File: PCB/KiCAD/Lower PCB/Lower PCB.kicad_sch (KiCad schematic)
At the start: 16 parts, among them J2 Conn_01x02, U1 ATmega328PB-A, Y1 Crystal

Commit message: Placed components on Lower PCB
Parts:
- R4: value 330 -> 10k
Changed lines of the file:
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@@
 			)
 		)
-		(property "Value" "330"
+		(property "Value" "10k"
 			(at 68.58 88.8999 0)
 			(effects

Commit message: More work to the lower PCB
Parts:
- removed Y1: Crystal, Crystal:Crystal_SMD_3225-4Pin_3.2x2.5mm_HandSoldering, symbol Device:Crystal
- added C31, C32: 100nF, Capacitor_SMD:C_0805_2012Metric_Pad1.18x1.45mm_HandSolder, symbol Device:C
- added D10, D11, D12, D13, D14, D15, D16, D17, D18, D19, D20, D21, D22, D23, D24, D5, D6, D7, D8, D9: LED, LED_SMD:LED_PLCC-2_3.4x3.0mm_KA, symbol Device:LED
- added IC1, IC2: ADG608BRZ, ADG608BRZ:SOIC127P600X175-16N, symbol ADG608BRZ:ADG608BRZ
- added Q1, Q10, Q11, Q12, Q13, Q14, Q15, Q16, Q2, Q3, Q4, Q5, Q6, Q7, Q8, Q9: SFH320, LED_SMD:LED_PLCC-2_3.4x3.0mm_KA, symbol Sensor_Optical:SFH320
- added R10, R14, R16, R18, R35, R36, R37, R38, R39, R40, R41, R42, R43, R44, R45, R46: 10k, Resistor_SMD:R_0805_2012Metric_Pad1.20x1.40mm_HandSolder, symbol Device:R
- added R11, R15, R17, R19, R20, R21, R22, R23, R24, R25, R26, R27, R28, R29, R30, R31, R32, R33, R34, R9: 330, Resistor_SMD:R_0805_2012Metric_Pad1.20x1.40mm_HandSolder, symbol Device:R
- added Y1: Crystal_GND24, Crystal:Crystal_SMD_5032-4Pin_5.0x3.2mm, symbol Device:Crystal_GND24
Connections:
- net +5V: now also C31.1, C32.1, IC1.13 (VDD), IC1.2 (EN), IC2.13 (VDD), IC2.2 (EN), Q1.1 (C), Q10.1 (C), Q11.1 (C), Q12.1 (C), Q13.1 (C), Q14.1 (C), Q15.1 (C), Q16.1 (C), Q2.1 (C), Q3.1 (C), Q4.1 (C), Q5.1 (C), Q6.1 (C), Q7.1 (C), Q8.1 (C), Q9.1 (C), R11.2, R15.2, R17.2, R19.2, R20.2, R21.2, R22.2, R23.2, R24.2, R25.2, R26.2, R27.2, R28.2, R29.2, R30.2, R31.2, R32.2, R33.2, R34.2, R9.2
- net GND: now also C31.2, C32.2, D10.1 (K), D11.1 (K), D12.1 (K), D13.1 (K), D14.1 (K), D15.1 (K), D16.1 (K), D17.1 (K), D18.1 (K), D19.1 (K), D20.1 (K), D21.1 (K), D22.1 (K), D23.1 (K), D24.1 (K), D5.1 (K), D6.1 (K), D7.1 (K), D8.1 (K), D9.1 (K), IC1.14 (GND), IC1.3 (VSS), IC2.14 (GND), IC2.3 (VSS), R10.1, R14.1, R16.1, R18.1, R35.1, R36.1, R37.1, R38.1, R39.1, R40.1, R41.1, R42.1, R43.1, R44.1, R45.1, R46.1
- net at C5.2, U1.8 (XTAL2/PB7): now also Y1.3
- net at C4.2, U1.7 (XTAL1/PB6): now also Y1.1
- new net: D7.2 (A), R15.1
- new net: IC1.4 (S1), Q1.2 (E), R10.2
- new net: D22.2 (A), R32.1
- new net: D23.2 (A), R33.1
- new net: D11.2 (A), R21.1
- new net: IC2.6 (S3), Q11.2 (E), R41.2
- new net: IC2.5 (S2), Q10.2 (E), R40.2
- new net: D19.2 (A), R29.1
- new net: D5.2 (A), R9.1
- new net: D14.2 (A), R24.1
- new net: IC1.5 (S2), Q2.2 (E), R14.2
- new net: D10.2 (A), R20.1
- new net: IC1.12 (S5), Q5.2 (E), R35.2
- new net: D13.2 (A), R23.1
- new net: IC2.7 (S4), Q12.2 (E), R42.2
- new net: IC2.11 (S6), Q14.2 (E), R44.2
- new net: IC1.9 (S8), Q8.2 (E), R38.2
- new net: D6.2 (A), R11.1
- new net: D9.2 (A), R19.1
- new net: D17.2 (A), R27.1
- new net: D21.2 (A), R31.1
- new net: D16.2 (A), R26.1
- new net: IC2.4 (S1), Q9.2 (E), R39.2
- new net: IC1.10 (S7), Q7.2 (E), R37.2
- new net: IC1.11 (S6), Q6.2 (E), R36.2
- new net: IC1.6 (S3), Q3.2 (E), R16.2
- new net: IC1.7 (S4), Q4.2 (E), R18.2
- new net: D8.2 (A), R17.1
- new net: D15.2 (A), R25.1
- new net: D12.2 (A), R22.1
- new net: D20.2 (A), R30.1
- new net: IC2.10 (S7), Q15.2 (E), R45.2
- new net: IC2.9 (S8), Q16.2 (E), R46.2
- new net: D24.2 (A), R34.1
- new net: D18.2 (A), R28.1
- new net: IC2.12 (S5), Q13.2 (E), R43.2

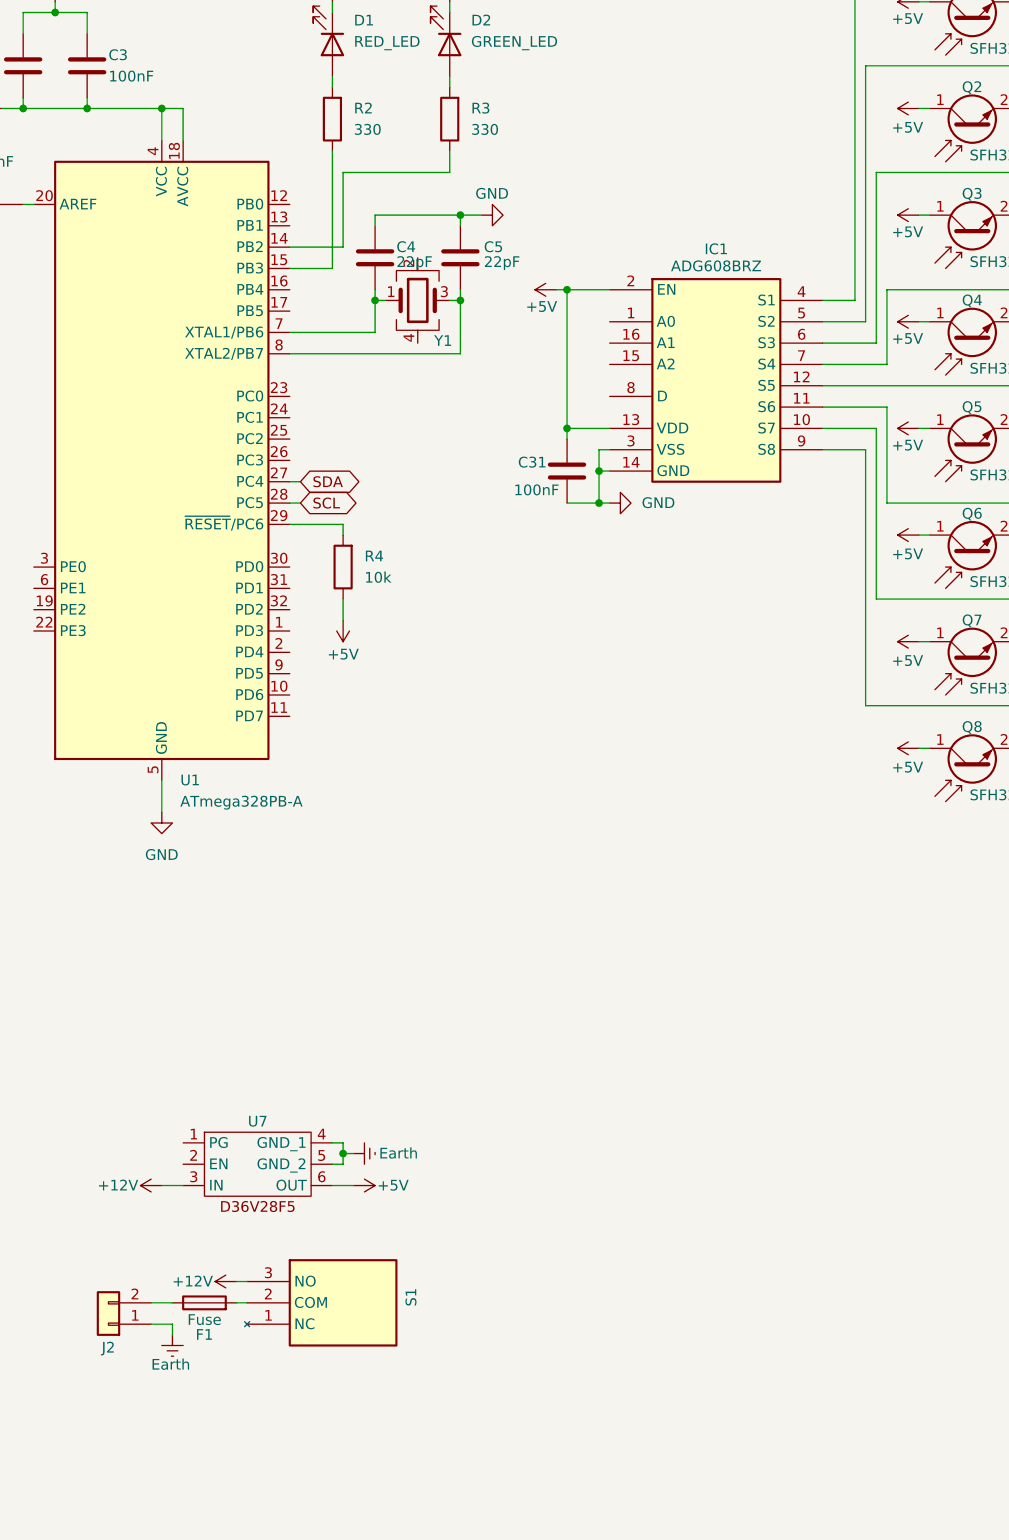
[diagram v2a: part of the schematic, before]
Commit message: Finished routing main motor controller connections and added connectors
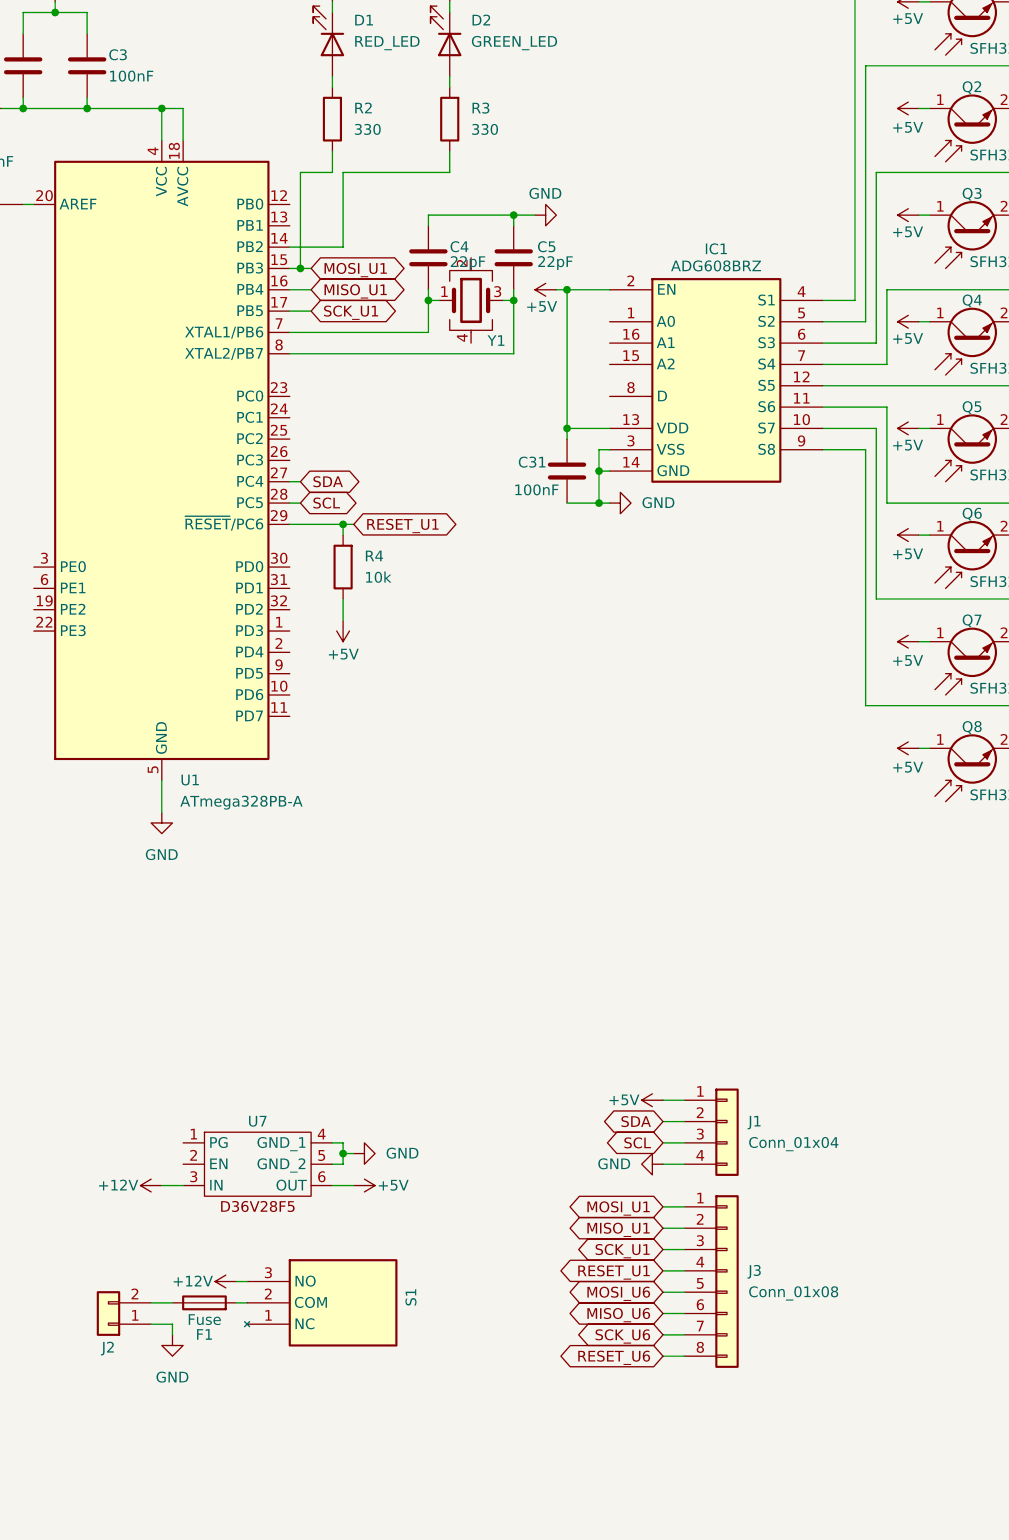
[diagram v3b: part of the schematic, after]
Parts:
- added J1: Conn_01x04, Connector_JST:JST_PH_B4B-PH-K_1x04_P2.00mm_Vertical, symbol Connector_Generic:Conn_01x04
- added J3: Conn_01x08, Connector_JST:JST_PH_B8B-PH-K_1x08_P2.00mm_Vertical, symbol Connector_Generic:Conn_01x08
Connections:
- net Earth is gone; now on net GND: J2.1 (Pin_1), U7.4 (GND_1), U7.5 (GND_2)
- net +5V: now also J1.1 (Pin_1)
- net GND: now also J1.4 (Pin_4)
- net SCL: now also J1.3 (Pin_3)
- net SDA: now also J1.2 (Pin_2)
- net RESET_U1: now reaches R4.2, U1.29 (~{RESET}/PC6)
- net RESET_U1: now also J3.4 (Pin_4)
- net MOSI_U1: now reaches R2.1, U1.15 (PB3)
- net MOSI_U1: now also J3.1 (Pin_1)
- net MISO_U1: now reaches U1.16 (PB4)
- net MISO_U1: now also J3.2 (Pin_2)
- net SCK_U1: now reaches U1.17 (PB5)
- net SCK_U1: now also J3.3 (Pin_3)
- new net MISO_U6: J3.6 (Pin_6)
- new net MOSI_U6: J3.5 (Pin_5)
- new net RESET_U6: J3.8 (Pin_8)
- new net SCK_U6: J3.7 (Pin_7)
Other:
- moved on the sheet: C4, C5, Y1

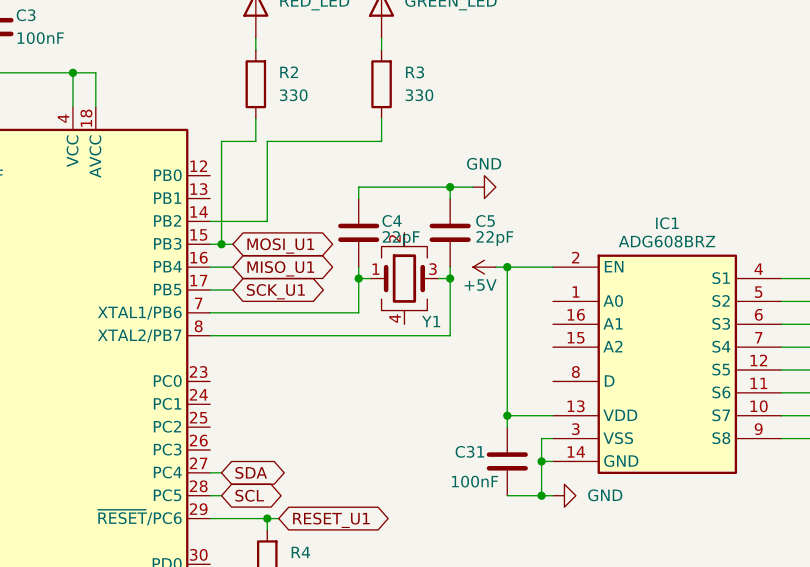
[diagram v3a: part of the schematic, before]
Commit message: More work to the Main PCB and refinement of Via sizes
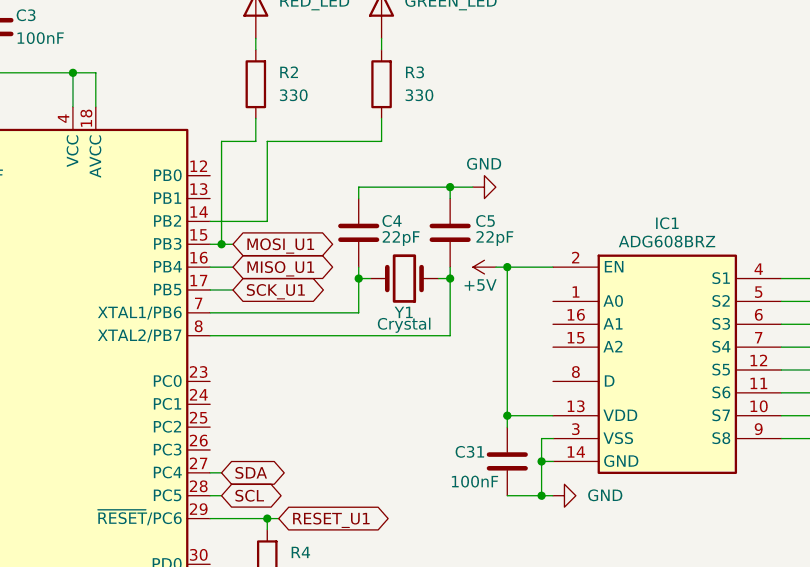
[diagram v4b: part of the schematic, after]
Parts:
- removed Y1: Crystal_GND24, Crystal:Crystal_SMD_5032-4Pin_5.0x3.2mm, symbol Device:Crystal_GND24
- added Y1: Crystal, Crystal:Crystal_SMD_HC49-SD, symbol Device:Crystal
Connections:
- net at C4.2, U1.7 (XTAL1/PB6): now also Y1.2
- net at C5.2, U1.8 (XTAL2/PB7): now also Y1.1
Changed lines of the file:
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@@
 	)
 	(symbol
-		(lib_id "Device:Crystal_GND24")
-		(at 81.28 55.88 0)
-		(unit 1)
-		(exclude_from_sim no)
-		(in_bom yes)
-		(on_board yes)
-		(dnp no)
-		(property "Reference" "Y1"
-			(at 84.328 60.706 0)
-			(effects
-				(font
-					(size 1.27 1.27)
-				)
-			)
-		)
-		(property "Value" "Crystal_GND24"
-			(at 92.71 51.9998 0)
-			(effects
-				(font
-					(size 1.27 1.27)
-				)
-				(hide yes)
-			)
-		)
-		(property "Footprint" "Crystal:Crystal_SMD_5032-4Pin_5.0x3.2mm"
-			(at 81.28 55.88 0)
-			(effects
-				(font
-					(size 1.27 1.27)
-				)
-				(hide yes)
-			)
-		)
-		(property "Datasheet" "~"
-			(at 81.28 55.88 0)
-			(effects
-				(font
-					(size 1.27 1.27)
-				)
-				(hide yes)
-			)
-		)
-		(property "Description" "Four pin crystal, GND on pins 2 and 4"
-			(at 81.28 55.88 0)
-			(effects
-				(font
-					(size 1.27 1.27)
-				)
-				(hide yes)
-			)
-		)
-		(pin "1"
-		)
-		(pin "4"
-		)
-		(pin "2"
-		)
-		(pin "3"
-		)
-		(instances
-			(project "Lower PCB"
-				(path "/ce5ddd0c-e3c7-41d2-82e8-7cf5c6a3a2a3"
-					(reference "Y1")
-					(unit 1)
-				)
-			)
-		)
-	)
-	(symbol
 		(lib_id "Device:R")
 		(at 66.04 87.63 180)
@@
 					(unit 1)
 				)
+			)
+		)
+	)
+	(symbol
+		(lib_id "Device:Crystal")
+		(at 81.28 55.88 180)
+		(unit 1)
+		(exclude_from_sim no)
+		(in_bom yes)
+		(on_board yes)
+		(dnp no)
+		(property "Reference" "Y1"
+			(at 81.28 59.69 0)
+			(effects
+				(font
+					(size 1.27 1.27)
+				)
+			)
+		)
+		(property "Value" "Crystal"
+			(at 81.28 60.96 0)
+			(effects
+				(font
+					(size 1.27 1.27)
+				)
+			)
+		)
+		(property "Footprint" "Crystal:Crystal_SMD_HC49-SD"
+			(at 81.28 55.88 0)
+			(effects
+				(font
+					(size 1.27 1.27)
+				)
+				(hide yes)
+			)
+		)
+		(property "Datasheet" "~"
+			(at 81.28 55.88 0)
+			(effects
+				(font
+					(size 1.27 1.27)
+				)
+				(hide yes)
+			)
+		)
+		(property "Description" "Two pin crystal"
+			(at 81.28 55.88 0)
+			(effects
+				(font
+					(size 1.27 1.27)
+				)
+				(hide yes)
+			)
+		)
+		(pin "2"
+		)
+		(pin "1"
+		)
+		(instances
+			(project "Lower PCB"
+				(path "/ce5ddd0c-e3c7-41d2-82e8-7cf5c6a3a2a3"
+					(reference "Y1")
+					(unit 1)
+				)
